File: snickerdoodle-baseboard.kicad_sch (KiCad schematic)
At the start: 0 parts

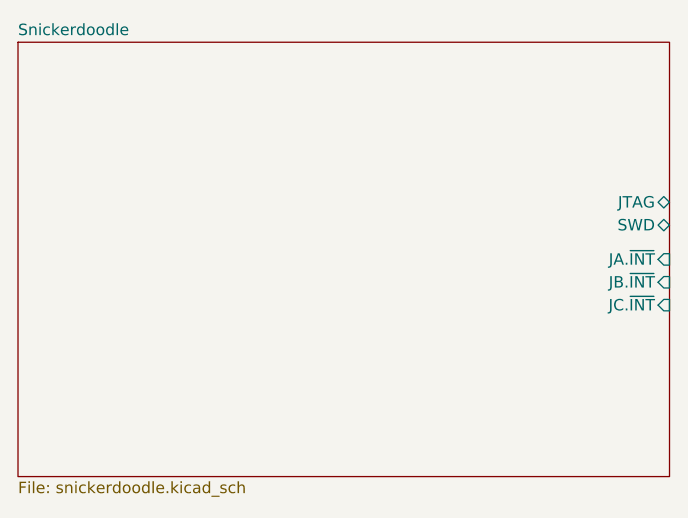
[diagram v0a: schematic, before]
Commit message: Fix bus names, add I2C, add footprints and 3D models
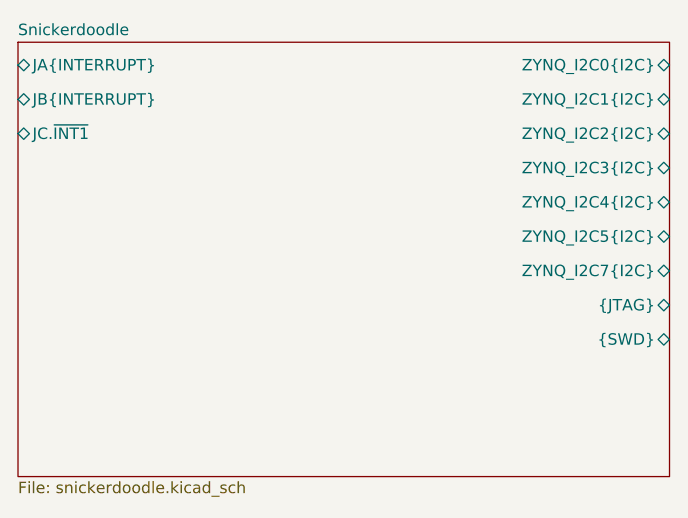
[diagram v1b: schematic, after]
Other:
- sheet Snickerdoodle ports: added JA{INTERRUPT}, JB{INTERRUPT}, JC.~INT1, ZYNQ_I2C0{I2C}, ZYNQ_I2C1{I2C}, ZYNQ_I2C2{I2C}, ZYNQ_I2C3{I2C}, ZYNQ_I2C4{I2C}, ZYNQ_I2C5{I2C}, ZYNQ_I2C7{I2C}, {JTAG}, {SWD}; removed JA.~INT, JB.~INT, JC.~INT, JTAG, SWD
- company: (none) -> Drawn by: Cameron McQuinn
- title: (none) -> Snickerdoodle Baseboard
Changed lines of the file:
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@@
   (page 3 2)
   (paper "B")
+  (title_block
+    (title "Snickerdoodle Baseboard")
+    (date "2020-06-24")
+    (rev "1.0")
+    (company "Drawn by: Cameron McQuinn")
+  )
   (sheet (at 85.09 64.77) (size 72.39 48.26)
     (stroke (width 0.001) (type solid) (color 132 0 132 1))
@@
       (effects (font (size 1.27 1.27)) (justify left top))
     )
-    (pin "JTAG" bidirectional (at 157.48 82.55 0)
+    (pin "{JTAG}" bidirectional (at 157.48 93.98 0)
       (effects (font (size 1.27 1.27)) (justify right))
     )
-    (pin "SWD" bidirectional (at 157.48 85.09 0)
+    (pin "{SWD}" bidirectional (at 157.48 97.79 0)
       (effects (font (size 1.27 1.27)) (justify right))
     )
-    (pin "JA.~INT" input (at 157.48 88.9 0)
+    (pin "ZYNQ_I2C2{I2C}" bidirectional (at 157.48 74.93 0)
       (effects (font (size 1.27 1.27)) (justify right))
     )
-    (pin "JC.~INT" input (at 157.48 93.98 0)
+    (pin "ZYNQ_I2C1{I2C}" bidirectional (at 157.48 71.12 0)
       (effects (font (size 1.27 1.27)) (justify right))
     )
-    (pin "JB.~INT" input (at 157.48 91.44 0)
+    (pin "ZYNQ_I2C0{I2C}" bidirectional (at 157.48 67.31 0)
       (effects (font (size 1.27 1.27)) (justify right))
+    )
+    (pin "ZYNQ_I2C3{I2C}" bidirectional (at 157.48 78.74 0)
+      (effects (font (size 1.27 1.27)) (justify right))
+    )
+    (pin "ZYNQ_I2C4{I2C}" bidirectional (at 157.48 82.55 0)
+      (effects (font (size 1.27 1.27)) (justify right))
+    )
+    (pin "ZYNQ_I2C5{I2C}" bidirectional (at 157.48 86.36 0)
+      (effects (font (size 1.27 1.27)) (justify right))
+    )
+    (pin "ZYNQ_I2C7{I2C}" bidirectional (at 157.48 90.17 0)
+      (effects (font (size 1.27 1.27)) (justify right))
+    )
+    (pin "JB{INTERRUPT}" bidirectional (at 85.09 71.12 180)
+      (effects (font (size 1.27 1.27)) (justify left))
+    )
+    (pin "JC.~INT1" bidirectional (at 85.09 74.93 180)
+      (effects (font (size 1.27 1.27)) (justify left))
+    )
+    (pin "JA{INTERRUPT}" bidirectional (at 85.09 67.31 180)
+      (effects (font (size 1.27 1.27)) (justify left))
     )
   )
   (symbol_instances
+    (path "/a32a7713-aceb-431f-82b6-7899cc3ddd29/08fc91e0-d17b-4470-a036-ebc456aa575c"
+      (reference "#PWR0101") (unit 1)
+    )
+    (path "/a32a7713-aceb-431f-82b6-7899cc3ddd29/1138c638-1d4c-47e6-82bd-88a45eb895a2"
+      (reference "#PWR0102") (unit 1)
+    )
+    (path "/a32a7713-aceb-431f-82b6-7899cc3ddd29/04dd64b4-3b36-41d1-b028-2494509baee3"
+      (reference "#PWR0103") (unit 1)
+    )
+    (path "/a32a7713-aceb-431f-82b6-7899cc3ddd29/a0fe4b1a-613d-4983-a1db-e5bcb782d807"
+      (reference "#PWR0104") (unit 1)
+    )
+    (path "/a32a7713-aceb-431f-82b6-7899cc3ddd29/912e424b-88a4-49b6-bccb-e0c55dd5390a"
+      (reference "#PWR0105") (unit 1)
+    )
+    (path "/a32a7713-aceb-431f-82b6-7899cc3ddd29/98a5fdfe-900b-4e5e-a7b9-3aae14bcaa54"
+      (reference "#PWR0106") (unit 1)
+    )
     (path "/a32a7713-aceb-431f-82b6-7899cc3ddd29/0109cf42-3133-42f6-973c-1300321b4dc6"
+      (reference "#PWR0107") (unit 1)
+    )
+    (path "/a32a7713-aceb-431f-82b6-7899cc3ddd29/cd66aca3-3023-490a-812a-a32c6ae271cb"
+      (reference "#PWR0108") (unit 1)
+    )
+    (path "/a32a7713-aceb-431f-82b6-7899cc3ddd29/03b7b80b-a7bb-4036-90e1-586a5b1258e5"
+      (reference "#PWR0109") (unit 1)
+    )
+    (path "/a32a7713-aceb-431f-82b6-7899cc3ddd29/485616be-00f5-4612-9b08-bbad43352e3c"
+      (reference "#PWR0110") (unit 1)
+    )
+    (path "/a32a7713-aceb-431f-82b6-7899cc3ddd29/76cca578-9d78-4f87-bd2b-d2db60cb20f8"
+      (reference "#PWR0111") (unit 1)
+    )
+    (path "/a32a7713-aceb-431f-82b6-7899cc3ddd29/3089b2c3-662c-4d0a-9585-dae07dfa01b2"
+      (reference "#PWR0112") (unit 1)
+    )
+    (path "/a32a7713-aceb-431f-82b6-7899cc3ddd29/763b31d8-d874-45bb-aee2-aae29ea7774e"
+      (reference "#PWR0113") (unit 1)
+    )
+    (path "/a32a7713-aceb-431f-82b6-7899cc3ddd29/34b52e9f-2866-4126-9df7-7fb23aaae287"
+      (reference "#PWR0114") (unit 1)
+    )
+    (path "/a32a7713-aceb-431f-82b6-7899cc3ddd29/97016788-c363-4899-9fd2-e117fa180900"
       (reference "#PWR?") (unit 1)
     )
-    (path "/a32a7713-aceb-431f-82b6-7899cc3ddd29/03b7b80b-a7bb-4036-90e1-586a5b1258e5"
-      (reference "#PWR?") (unit 1)
-    )
-    (path "/a32a7713-aceb-431f-82b6-7899cc3ddd29/04dd64b4-3b36-41d1-b028-2494509baee3"
-      (reference "#PWR?") (unit 1)
-    )
-    (path "/a32a7713-aceb-431f-82b6-7899cc3ddd29/08fc91e0-d17b-4470-a036-ebc456aa575c"
-      (reference "#PWR?") (unit 1)
-    )
-    (path "/a32a7713-aceb-431f-82b6-7899cc3ddd29/1138c638-1d4c-47e6-82bd-88a45eb895a2"
-      (reference "#PWR?") (unit 1)
-    )
-    (path "/a32a7713-aceb-431f-82b6-7899cc3ddd29/3089b2c3-662c-4d0a-9585-dae07dfa01b2"
-      (reference "#PWR?") (unit 1)
-    )
-    (path "/a32a7713-aceb-431f-82b6-7899cc3ddd29/34b52e9f-2866-4126-9df7-7fb23aaae287"
-      (reference "#PWR?") (unit 1)
-    )
-    (path "/a32a7713-aceb-431f-82b6-7899cc3ddd29/485616be-00f5-4612-9b08-bbad43352e3c"
-      (reference "#PWR?") (unit 1)
-    )
-    (path "/a32a7713-aceb-431f-82b6-7899cc3ddd29/763b31d8-d874-45bb-aee2-aae29ea7774e"
-      (reference "#PWR?") (unit 1)
-    )
-    (path "/a32a7713-aceb-431f-82b6-7899cc3ddd29/76cca578-9d78-4f87-bd2b-d2db60cb20f8"
-      (reference "#PWR?") (unit 1)
-    )
-    (path "/a32a7713-aceb-431f-82b6-7899cc3ddd29/912e424b-88a4-49b6-bccb-e0c55dd5390a"
-      (reference "#PWR?") (unit 1)
-    )
-    (path "/a32a7713-aceb-431f-82b6-7899cc3ddd29/98a5fdfe-900b-4e5e-a7b9-3aae14bcaa54"
-      (reference "#PWR?") (unit 1)
-    )
-    (path "/a32a7713-aceb-431f-82b6-7899cc3ddd29/a0fe4b1a-613d-4983-a1db-e5bcb782d807"
-      (reference "#PWR?") (unit 1)
-    )
-    (path "/a32a7713-aceb-431f-82b6-7899cc3ddd29/cd66aca3-3023-490a-812a-a32c6ae271cb"
-      (reference "#PWR?") (unit 1)
-    )
